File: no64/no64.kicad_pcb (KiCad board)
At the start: 2 copper layers, 0 parts

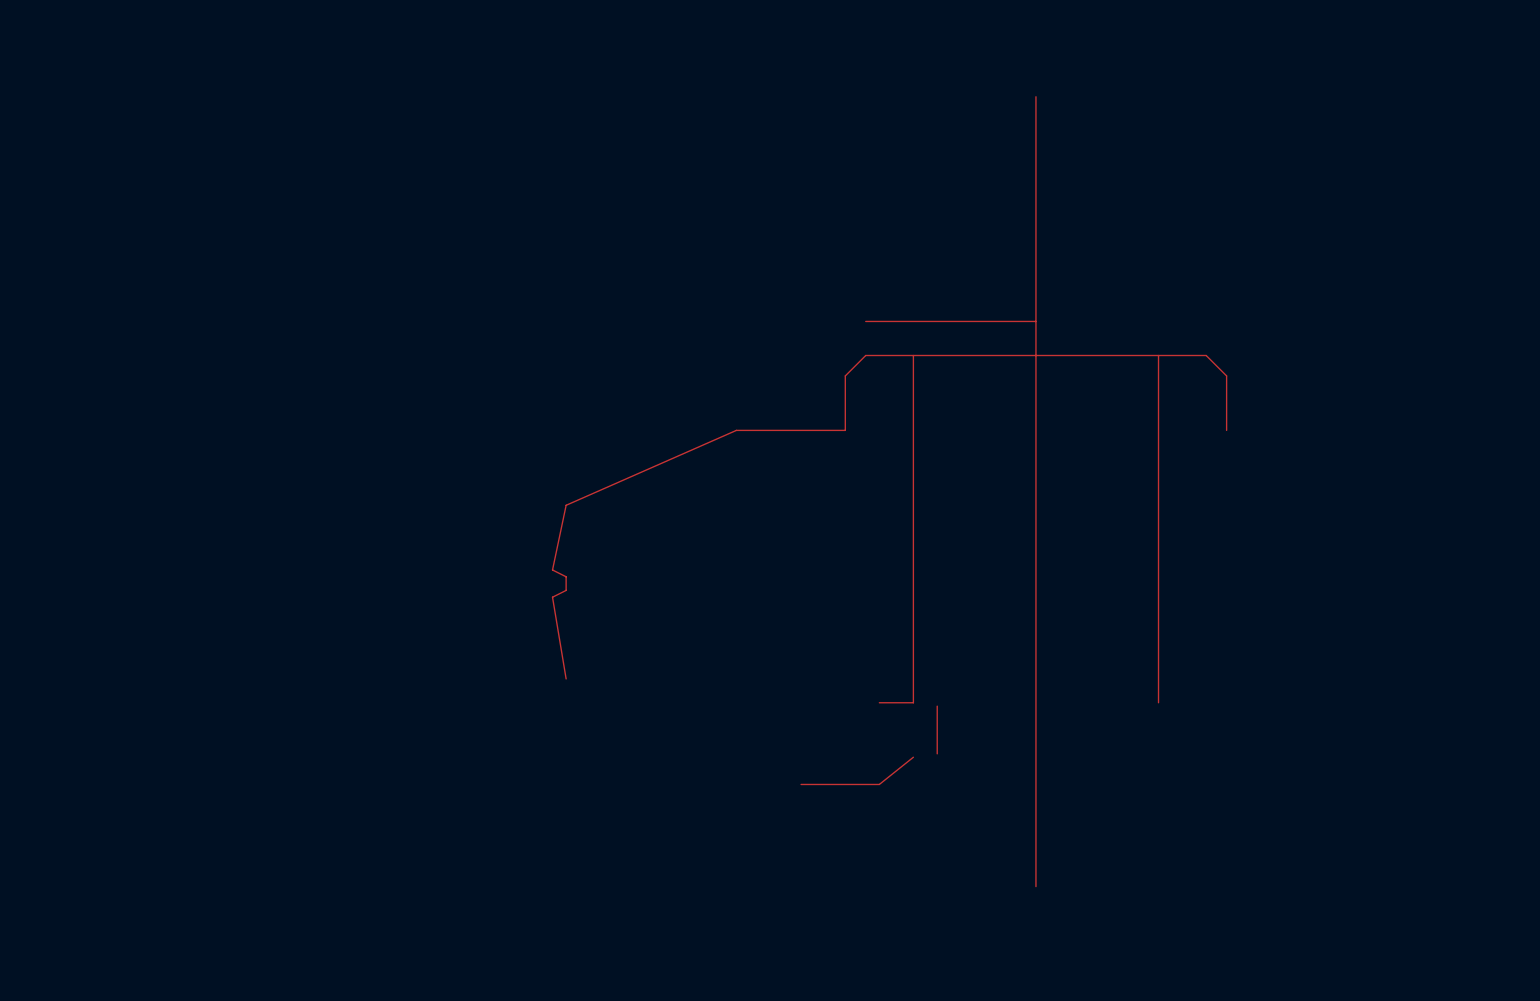
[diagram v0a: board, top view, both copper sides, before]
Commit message: Finish PCB outline
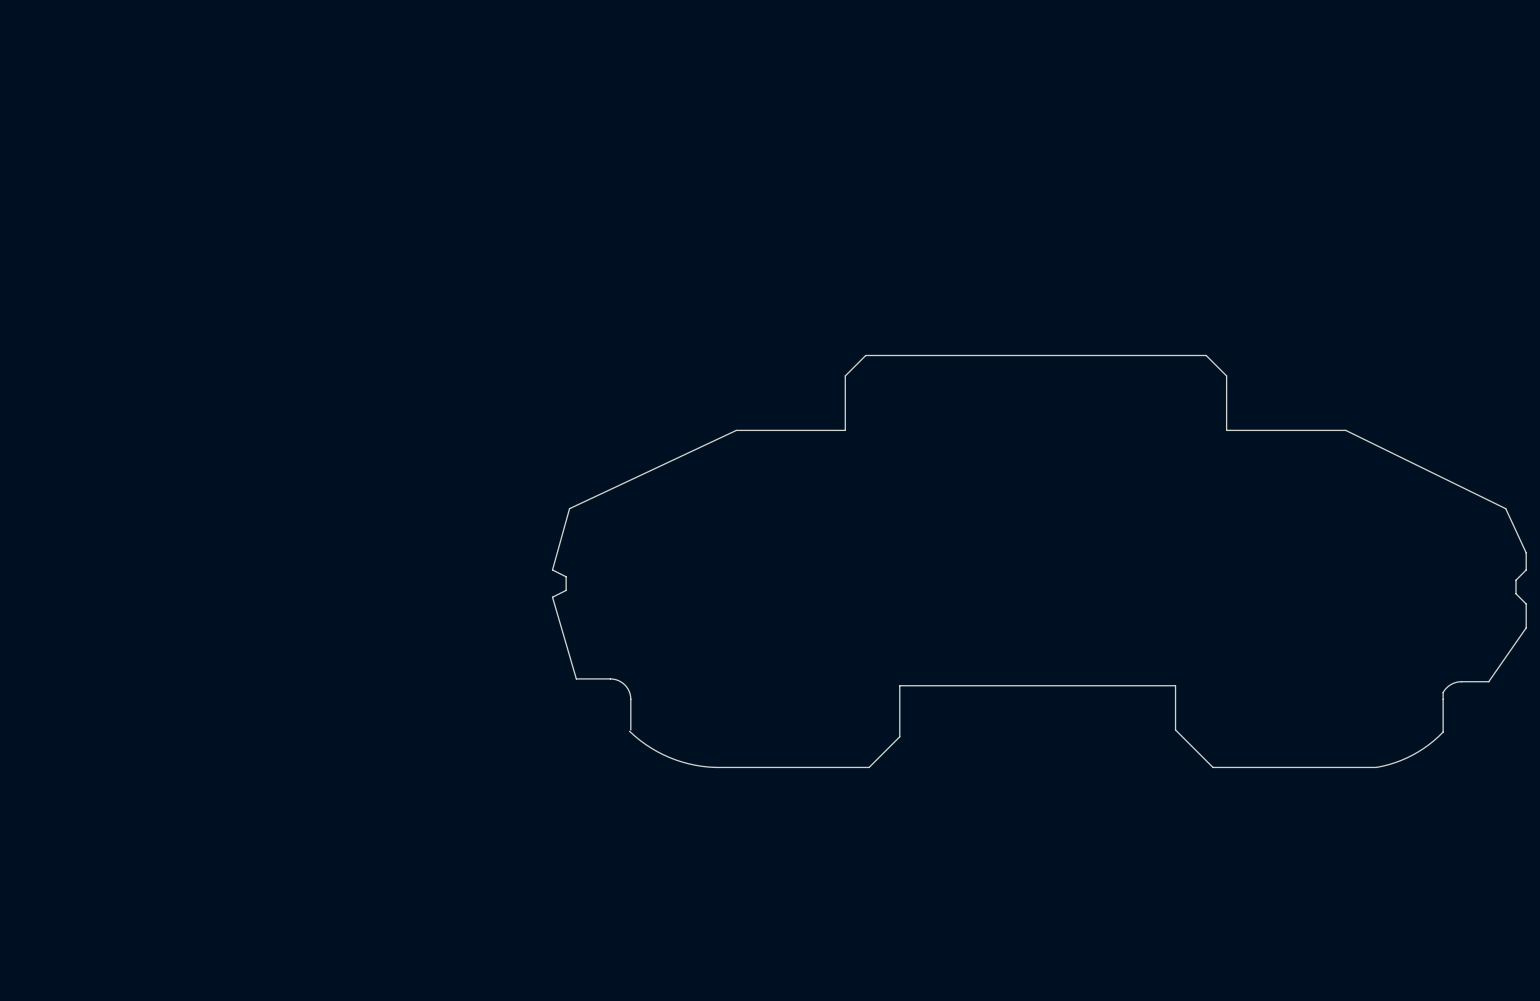
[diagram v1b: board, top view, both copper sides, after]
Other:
- board outline added: 143 x 60.5 mm

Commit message: More WIP
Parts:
- added ?: , , F.Cu at (195.8, 100.2)
- added ?: , , F.Cu at (181.8, 93.8)
- added ?: , , F.Cu at (200.0, 90.5)
- added ?: , , F.Cu at (198.0, 79.5)
- added ?: , , F.Cu at (189.7, 81.3)
- added ?: , , F.Cu at (214.8, 84.3)
- added ?: , , F.Cu at (187.5, 102.0)
- added ?: , , F.Cu at (208.0, 70.5)
- added ?: , , F.Cu at (213.0, 76.0)
- added ?: , , F.Cu at (199.7, 72.3)
- added ?: , , F.Cu at (180.0, 85.5)
- added ?: , , F.Cu at (208.3, 88.7)
- added J1: Analog Stick, Connector_JST:JST_PH_S6B-PH-K_1x06_P2.00mm_Horizontal, F.Cu at (2.48, 1.88)
- added J1: Analog Stick, Connector_JST:JST_PH_S6B-PH-K_1x06_P2.00mm_Horizontal, B.Cu at (114.0, 103.0)
- added J2: Conn_01x04_Socket, Connector_PinHeader_2.00mm:PinHeader_1x04_P2.00mm_Vertical, F.Cu at (174.5, 81.0)
- added REF**: MountingHole_2.2mm_M2, MountingHole:MountingHole_2.2mm_M2, F.Cu at (130.5, 57.5)
- added REF**: MountingHole_2.7mm, MountingHole:MountingHole_2.7mm, F.Cu at (186.0, 72.5)
- added REF**: MountingHole_2.1mm, MountingHole:MountingHole_2.1mm, F.Cu at (175.0, 67.5)
- added REF**: MountingHole_2.1mm, MountingHole:MountingHole_2.1mm, F.Cu at (204.0, 80.5)
- added REF**: MountingHole_2.1mm, MountingHole:MountingHole_2.1mm, F.Cu at (158.0, 91.0)
- added REF**: MountingHole_2.1mm, MountingHole:MountingHole_2.1mm, F.Cu at (144.0, 91.0)
- added REF**: MountingHole_2.7mm, MountingHole:MountingHole_2.7mm, F.Cu at (115.0, 72.0)
- added REF**: MountingHole_2.1mm, MountingHole:MountingHole_2.1mm, F.Cu at (192.0, 90.0)
- added REF**: MountingHole_2.2mm_M2, MountingHole:MountingHole_2.2mm_M2, F.Cu at (171.0, 57.5)
- added REF**: MountingHole_2.1mm, MountingHole:MountingHole_2.1mm, F.Cu at (181.5, 67.5)
- added SW10: Cup, PhobGCC_2_0_0_footprints:Dpad_Contact_TL3315NF_2, F.Cu at (102.0, 76.5)
- added SW11: Dright, PhobGCC_2_0_0_footprints:Dpad_Contact_TL3315NF_2, F.Cu at (111.5, 86.0)
- added SW11: Cright, PhobGCC_2_0_0_footprints:Dpad_Contact_TL3315NF_2, F.Cu at (151.0, 91.5)
- added SW12: Cdown, PhobGCC_2_0_0_footprints:Dpad_Contact_TL3315NF_2, F.Cu at (102.2, 96.0)
- added SW9: Cleft, PhobGCC_2_0_0_footprints:Dpad_Contact_TL3315NF_2, F.Cu at (93.0, 86.0)
- added U2: AMS1117-3.3, Package_TO_SOT_SMD:SOT-223-3_TabPin2, F.Cu at (111.4, 137.8)
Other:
- outline, holes or cut-outs redrawn

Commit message: add button pads from phob (can almost all of of these), use better pico model
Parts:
- removed ? (x12): , 
- removed REF** (x2): MountingHole_2.2mm_M2, MountingHole:MountingHole_2.2mm_M2
- removed REF** (x2): MountingHole_2.7mm, MountingHole:MountingHole_2.7mm
- removed REF** (x6): MountingHole_2.1mm, MountingHole:MountingHole_2.1mm
- removed the SW11 at (111.5, 86.0)
- removed the SW11 at (151.0, 91.5)
- added A1: RaspberryPi_Pico, MCU_Module_RaspberryPi_Pico:RaspberryPi_Pico_Common_SMD, B.Cu at (145.5, 74.9)
- added D5: CUS10S30,H3F, Diode_SMD:D_SOD-323, F.Cu at (179.0, 74.5)
- added H1: 5.0mm, MountingHole:MountingHole_5mm, F.Cu at (130.5, 57.5)
- added H2: 5.0mm, MountingHole:MountingHole_5mm, F.Cu at (171.0, 57.5)
- added H3: 5.0mm, MountingHole:MountingHole_5mm, F.Cu at (186.5, 72.0)
- added H4: 2.0mm, MountingHole:MountingHole_2mm, F.Cu at (181.5, 67.5)
- added H5: 2.0mm, MountingHole:MountingHole_2mm, F.Cu at (192.0, 90.0)
- added H5: 2.0mm, MountingHole:MountingHole_2mm, F.Cu at (204.0, 80.5)
- added H5: 2.0mm, MountingHole:MountingHole_2mm, F.Cu at (175.5, 67.5)
- added H6: 2.0mm, MountingHole:MountingHole_2mm, F.Cu at (158.0, 91.0)
- added H7: 2.0mm, MountingHole:MountingHole_2mm, F.Cu at (144.5, 91.0)
- added H8: 5.0mm, MountingHole:MountingHole_5mm, F.Cu at (115.5, 72.0)
- added SW11: Cright, PhobGCC_2_0_0:Dpad_Contact_TL3315NF_2_ZigZag, F.Cu at (213.5, 80.5)
- added SW2: A, PhobGCC_2_0_0:ABXY_Contact_Omron_Switch_Circley, F.Cu at (192.0, 101.5)
- added SW3: B, PhobGCC_2_0_0:ABXY_Contact_Omron_Switch_Circley, F.Cu at (180.5, 89.5)
- added SW4: Dleft, PhobGCC_2_0_0:Dpad_Contact_TL3315NF_2_ZigZag, F.Cu at (92.5, 85.5)
- added SW5: Dup, PhobGCC_2_0_0:Dpad_Contact_TL3315NF_2_ZigZag, F.Cu at (102.0, 76.5)
- added SW6: Dright, PhobGCC_2_0_0:Dpad_Contact_TL3315NF_2_ZigZag, F.Cu at (111.5, 85.5)
- added SW7: Ddown, PhobGCC_2_0_0:Dpad_Contact_TL3315NF_2_ZigZag, F.Cu at (102.0, 95.5)
- added SW8: START, PhobGCC_2_0_0:Dpad_Contact_TL3315NF_2_ZigZag, F.Cu at (151.2, 91.1)
- SW10, SW12, SW9: footprint PhobGCC_2_0_0_footprints:Dpad_Contact_TL3315NF_2 -> PhobGCC_2_0_0:Dpad_Contact_TL3315NF_2_ZigZag
- moved SW10 102.1 mm to (204.0, 71.0), turned to 0 degrees
- moved SW12 102.0 mm to (204.0, 89.7), turned to 0 degrees
- moved SW9 101.6 mm to (194.5, 80.5), turned to 0 degrees
- moved U2 16.1 mm to (112.7, 121.8)

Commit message: Add pico 3d model, add L/R/START to PCB
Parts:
- removed the J1 at (114.0, 103.0)
- removed SW8: START, PhobGCC_2_0_0:Dpad_Contact_TL3315NF_2_ZigZag
- added L1: Conn_01x02, Connector_PinSocket_2.00mm:PinSocket_1x02_P2.00mm_Vertical, F.Cu at (106.5, 64.0)
- added R1: Conn_01x02, Connector_PinSocket_2.00mm:PinSocket_1x02_P2.00mm_Vertical, F.Cu at (195.0, 63.5)
- added START3: Conn_01x02, Connector_PinSocket_2.00mm:PinSocket_1x02_P2.00mm_Vertical, F.Cu at (132.5, 91.0)
- J1: moved to B.Cu
- moved J1 150.1 mm to (113.5, 103.0)

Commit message: Rotate MCU, fix START/Z, misc cleanup
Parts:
- removed START3: Conn_01x02, Connector_PinSocket_2.00mm:PinSocket_1x02_P2.00mm_Vertical
- removed U2: AMS1117-3.3, Package_TO_SOT_SMD:SOT-223-3_TabPin2
- added SW8: START, PhobGCC_2_0_0:Dpad_Contact_TL3315NF_2_ZigZag, F.Cu at (150.8, 91.0)
- added Z3: Conn_01x02, Connector_PinSocket_2.00mm:PinSocket_1x02_P2.00mm_Vertical, F.Cu at (164.5, 90.5)
- SW2, SW3: footprint PhobGCC_2_0_0:ABXY_Contact_Omron_Switch_Circley -> PhobGCC_2_0_0:Dpad_Contact_TL3315NF_2_ZigZag
- moved D5 9.01 mm to (184.0, 82.0)
- moved J2 3.03 mm to (177.5, 81.0)
- moved A1 2.51 mm to (147.3, 76.6), turned to -80 degrees
- moved SW3 0.71 mm to (181.0, 90.0), turned to 180 degrees
- moved SW2 0.50 mm to (192.0, 101.0), turned to 180 degrees
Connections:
- A1 pad 24: unconnected-(A1-GPIO18-Pad24) -> /Z
